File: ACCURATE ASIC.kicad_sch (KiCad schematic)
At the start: 75 parts, among them IC12 ACCURATE_2A_JLCC28, IC13 DAC7578SRGE, IC14 CERN_aCCURATE2_A_Chip1, IC15 LM8272MMX, IC16 SHT41-AD1B, IC17 LM8272MMX, IC18 ADS1114IDGS, J17 SAMTEC_HTSW-103-23-L-D, J18 SAMTEC_HTSW-103-23-L-D, SW10 HARWIN_M50-1900005, SW11 HARWIN_M50-1900005, SW8 HARWIN_M50-1900005, SW9 HARWIN_M50-1900005

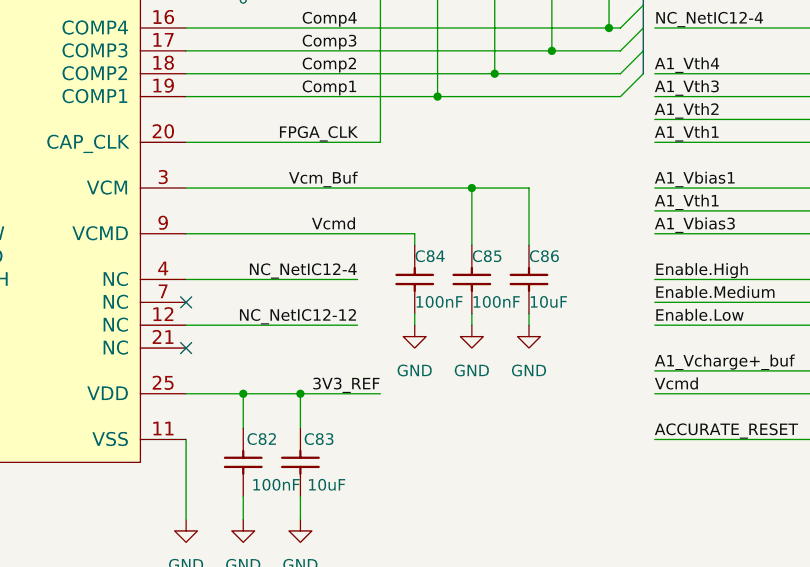
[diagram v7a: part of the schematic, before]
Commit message: Rename FPGA_PROG bus for mor clarity + small changes
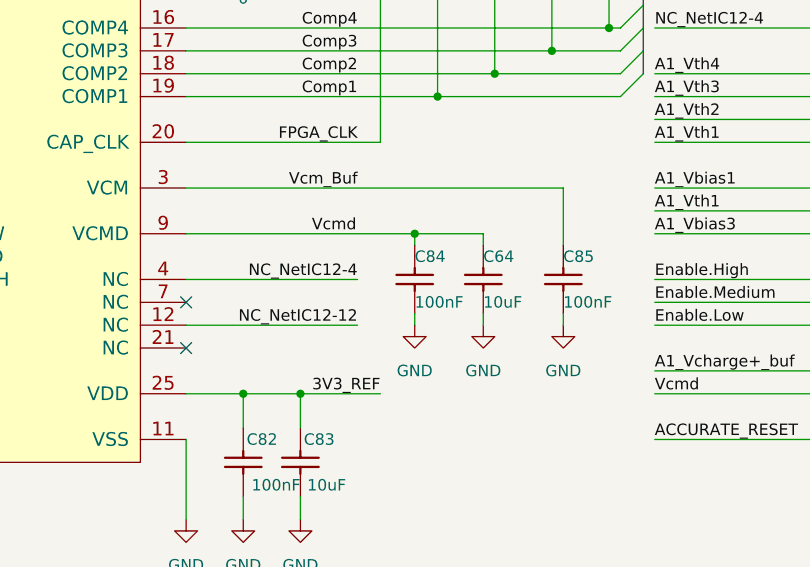
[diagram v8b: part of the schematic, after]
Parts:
- removed C86: CC0603_10UF_25V_20%_X5R, Capacitors SMD:CAPC1709X100N, symbol Capacitors SMD:CC0603_10UF_25V_20%_X5R
- added C64: CC0603_10UF_25V_20%_X5R, Capacitors SMD:CAPC1709X100N, symbol Capacitors SMD:CC0603_10UF_25V_20%_X5R
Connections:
- net GND: now also C64.2
- net Vcmd: now also C64.1
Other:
- moved on the sheet: C85
